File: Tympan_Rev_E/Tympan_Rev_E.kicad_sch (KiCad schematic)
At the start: 91 parts, among them IC1 BC127, J1 SJ-3523-SMT-TR, J2 SJ-3524-SMT-TR-PI, J3 Conn_01x06, J4 Qwiik Connector, J5 SMT, J6 SMT, P1 CONN_01X06, P2 CONN_01X06, P3 CONN_01X06, P4 CONN_01X06, P6 CONN_01X01, P7 CONN_01X01, P8 CONN_01X01, SW1 CL-SB-22A, SW2 SW_Push, U1 MCP73831, U2 TLV320AIC3206IRSBT, U3 74LVC1G66, U4 LP5907MFX-1.8, U5 Teensy4.1, U6 LC709203

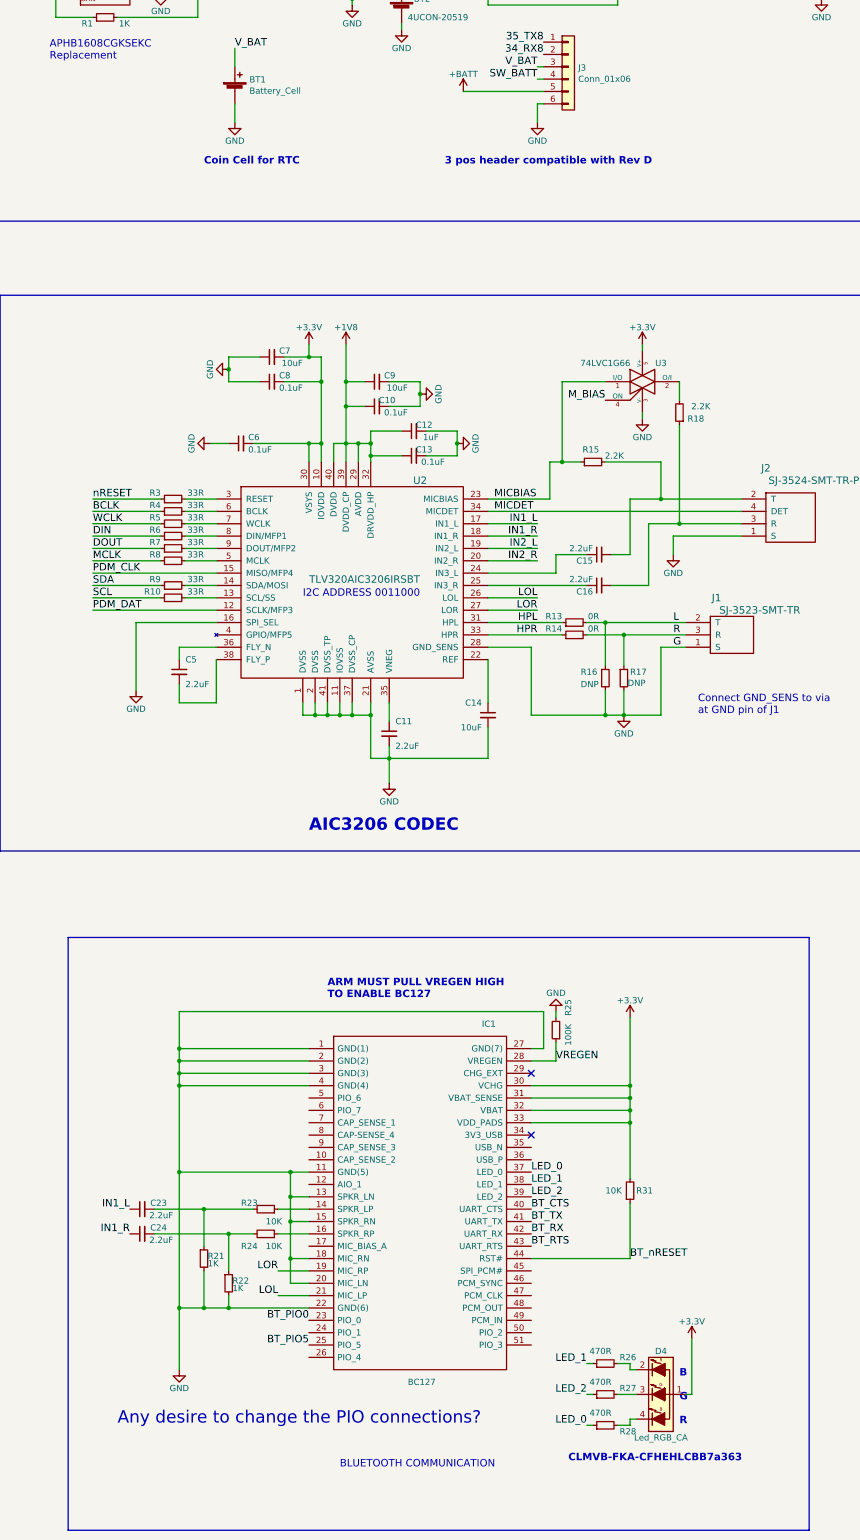
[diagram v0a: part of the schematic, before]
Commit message: Swapped out the BLE module
Replace the BC127 with the MDBT50Q-1MV2 nRF52840 module
The new module will be targeted as an Adafriut nRF52840 Feather Express
Made basic functional connections
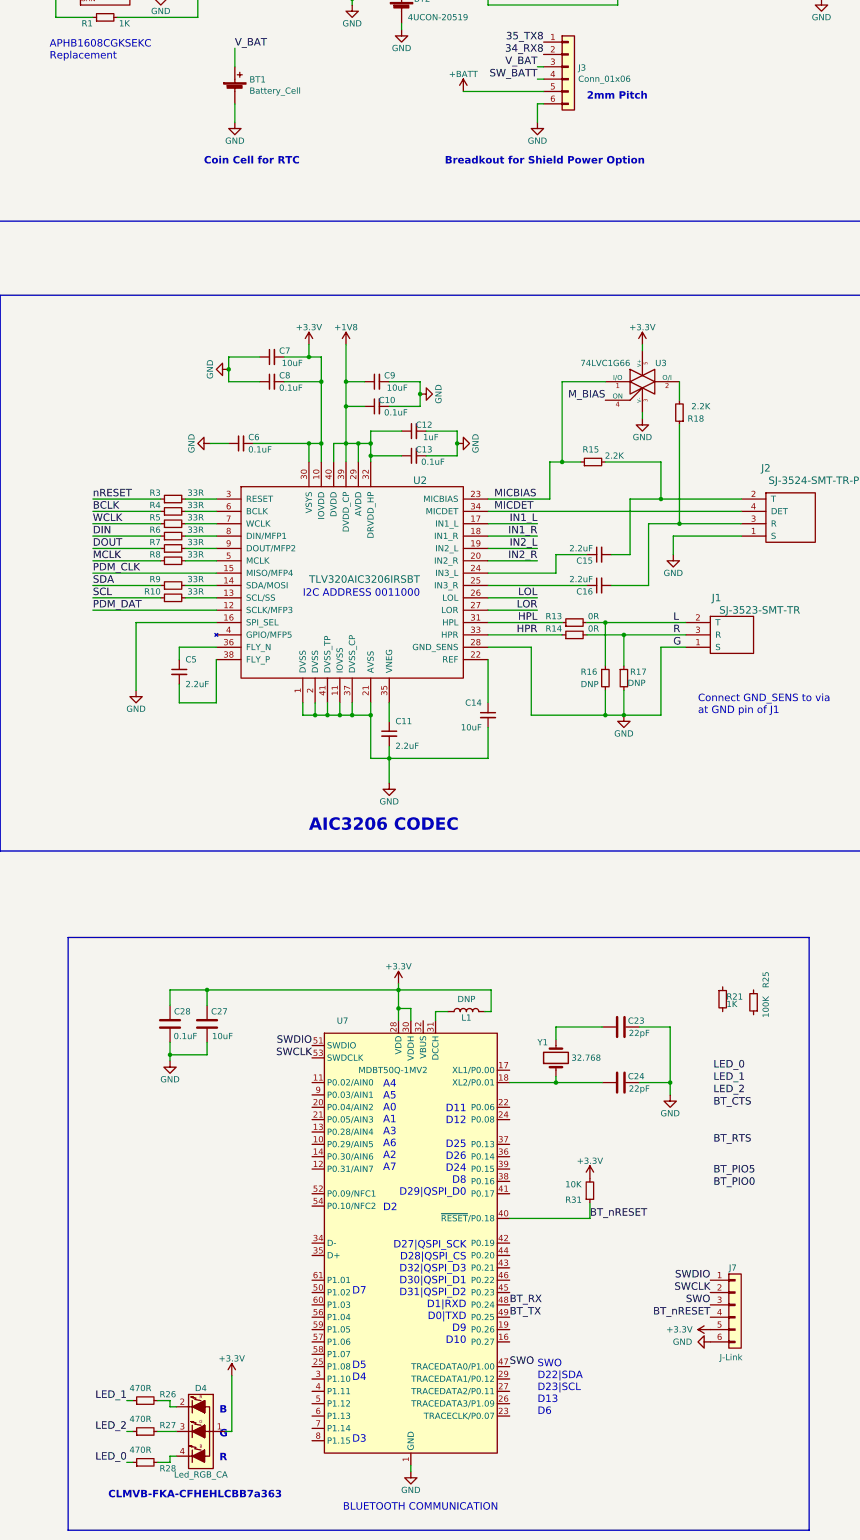
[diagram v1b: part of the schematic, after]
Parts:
- removed C23, C24: 2.2uF, Capacitor_SMD:C_0402_1005Metric, symbol Device:C_Small
- removed IC1: BC127, Tympan:BC127, symbol Tympan:BC127
- removed R22: 1K, Resistor_SMD:R_0402_1005Metric, symbol Device:R_Small
- removed R23, R24: 10K, Resistor_SMD:R_0402_1005Metric, symbol Device:R_Small
- added C23, C24: 22pF, symbol Device:C
- added C27: 10uF, symbol Device:C
- added C28: 0.1uF, symbol Device:C
- added J7: J-Link, symbol Connector_Generic:Conn_01x06
- added L1: DNP, symbol Device:L
- added U7: MDBT50Q-1MV2, RF_Module:Raytac_MDBT50Q, symbol RF_Module:MDBT50Q-1MV2
- added Y1: 32.768, symbol Device:Crystal
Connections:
- net +3.3V: now also C27.2, C28.2, J7.5 (Pin_5), L1.2, U7.28 (VDD), U7.30 (VDDH)
- net BT_RX: now also U7.48 (P0.24)
- net BT_TX: now also U7.49 (P0.25)
- net BT_nRESET: now also J7.4 (Pin_4), U7.40 (~{RESET}/P0.18)
- net GND: now also C23.2, C24.2, C27.1, C28.1, J7.6 (Pin_6), U7.1 (GND), U7.15 (GND), U7.2 (GND), U7.33 (GND), U7.55 (GND); no longer R21.2, R25.2
- net VREGEN: no longer R25.1
- new net: L1.1, U7.31 (DCCH)
- new net: C24.1, U7.18 (XL2/P0.01), Y1.1
- new net: C23.1, Y1.2
- new net SWCLK: J7.2 (Pin_2), U7.53 (SWDCLK)
- new net SWDIO: J7.1 (Pin_1), U7.51 (SWDIO)
- new net SWO: J7.3 (Pin_3), U7.47 (TRACEDATA0/P1.00)
- no-connect marks 22 -> 20
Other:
- note added: "2mm Pitch"
- note added: "A4 A5 A0 A1 A3 A6 A2 A7"
- note added: "Breadkout for Shield Power Option"
- note added: "D11 D12 D25 D26 D24 D8 D29|QSPI_D0"
- note added: "D2"
- note added: "D27|QSPI_SCK D28|QSPI_CS D32|QSPI_D3 D30|QSPI_D1 D31|QSPI_D2 D1|RXD D0|TXD D9 D10"
- note added: "D3"
- note added: "D5 D4"
- note added: "D7"
- note added: "SWO D22|SDA D23|SCL D13 D6"
- note removed: "3 pos header compatible with Rev D"
- note removed: "ARM MUST PULL VREGEN HIGH TO ENABLE BC127"
- note removed: "Any desire to change the PIO connections?"
- moved on the sheet: D4, R21, R25, R26, R27, R28, R31

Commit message: Revert "Swapped out the BLE module"
This reverts commit 95fca984de24e2c498e4892b05c2135819655856.
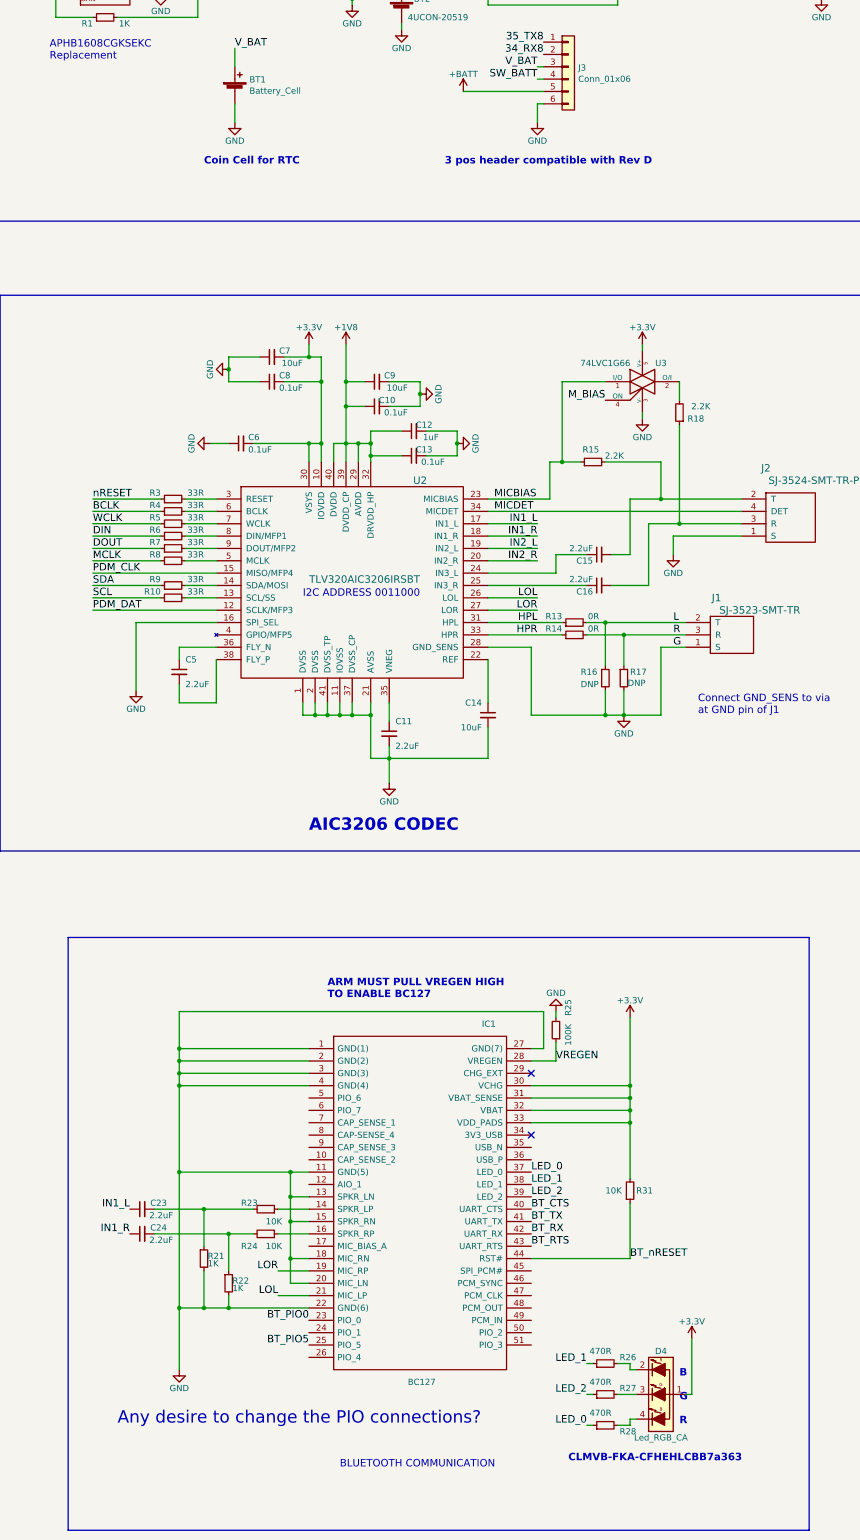
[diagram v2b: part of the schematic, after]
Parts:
- removed C23, C24: 22pF, symbol Device:C
- removed C27: 10uF, symbol Device:C
- removed C28: 0.1uF, symbol Device:C
- removed J7: J-Link, symbol Connector_Generic:Conn_01x06
- removed L1: DNP, symbol Device:L
- removed U7: MDBT50Q-1MV2, RF_Module:Raytac_MDBT50Q, symbol RF_Module:MDBT50Q-1MV2
- removed Y1: 32.768, symbol Device:Crystal
- added C23, C24: 2.2uF, Capacitor_SMD:C_0402_1005Metric, symbol Device:C_Small
- added IC1: BC127, Tympan:BC127, symbol Tympan:BC127
- added R22: 1K, Resistor_SMD:R_0402_1005Metric, symbol Device:R_Small
- added R23, R24: 10K, Resistor_SMD:R_0402_1005Metric, symbol Device:R_Small
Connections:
- net +3.3V: now also IC1.30 (VCHG), IC1.31 (VBAT_SENSE), IC1.32 (VBAT), IC1.33 (VDD_PADS)
- net BT_CTS: now also IC1.40 (UART_CTS)
- net BT_PIO0: now also IC1.23 (PIO_0)
- net BT_PIO5: now also IC1.25 (PIO_5)
- net BT_RTS: now also IC1.43 (UART_RTS)
- net BT_RX: now also IC1.42 (UART_RX)
- net BT_TX: now also IC1.41 (UART_TX)
- net BT_nRESET: now also IC1.44 (RST#)
- net GND: now also R21.2, R25.2, IC1.1 (GND(1)), IC1.11 (GND(5)), IC1.13 (SPKR_LN), IC1.15 (SPKR_RN), IC1.18 (MIC_RN), IC1.2 (GND(2)), IC1.20 (MIC_LN), IC1.22 (GND(6)), IC1.27 (GND(7)), IC1.3 (GND(3)), IC1.4 (GND(4)), R22.2
- net IN1_L: now also C23.1
- net IN1_R: now also C24.1
- net LED_0: now also IC1.37 (LED_0)
- net LED_1: now also IC1.38 (LED_1)
- net LED_2: now also IC1.39 (LED_2)
- net LOL: now also IC1.21 (MIC_LP)
- net LOR: now also IC1.19 (MIC_RP)
- net VREGEN: now also R25.1, IC1.28 (VREGEN)
- net at R21.1: now also C23.2, R23.2
- new net: IC1.14 (SPKR_LP), R23.1
- new net: IC1.16 (SPKR_RP), R24.1
- new net: C24.2, R22.1, R24.2
- no-connect marks 20 -> 22
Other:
- note added: "3 pos header compatible with Rev D"
- note added: "ARM MUST PULL VREGEN HIGH TO ENABLE BC127"
- note added: "Any desire to change the PIO connections?"
- note removed: "2mm Pitch"
- note removed: "A4 A5 A0 A1 A3 A6 A2 A7"
- note removed: "Breadkout for Shield Power Option"
- note removed: "D11 D12 D25 D26 D24 D8 D29|QSPI_D0"
- note removed: "D2"
- note removed: "D27|QSPI_SCK D28|QSPI_CS D32|QSPI_D3 D30|QSPI_D1 D31|QSPI_D2 D1|RXD D0|TXD D9 D10"
- note removed: "D3"
- note removed: "D5 D4"
- note removed: "D7"
- note removed: "SWO D22|SDA D23|SCL D13 D6"
- moved on the sheet: D4, R21, R25, R26, R27, R28, R31
